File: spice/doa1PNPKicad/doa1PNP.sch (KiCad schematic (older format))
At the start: 27 parts, among them Q1 BC547, Q2 BC557, Q3 BC557, Q4 BC557, Q5 BC547, Q6 BC557, Q7 BC547

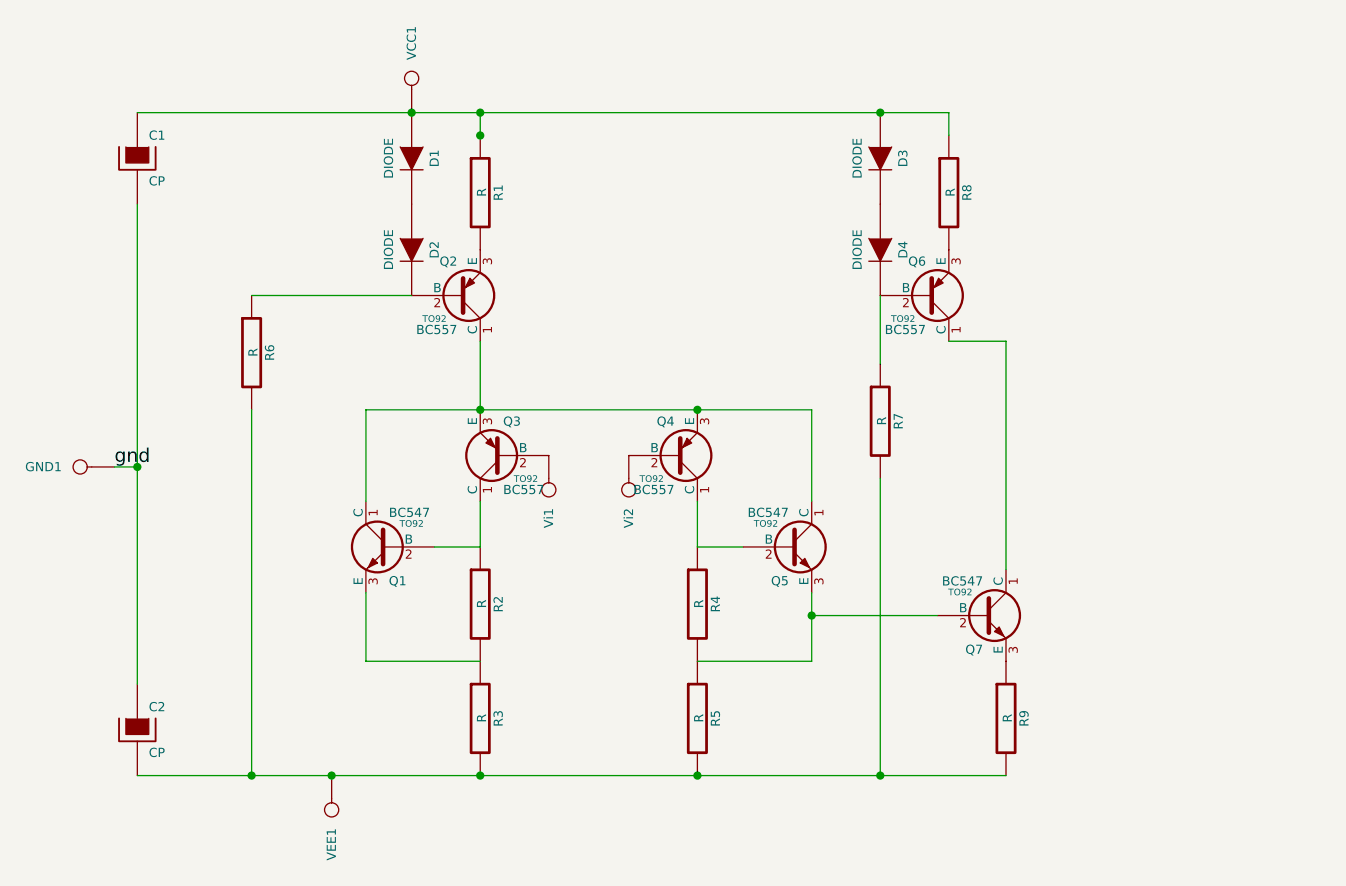
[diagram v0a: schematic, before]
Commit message: multiple current source doa1PNP
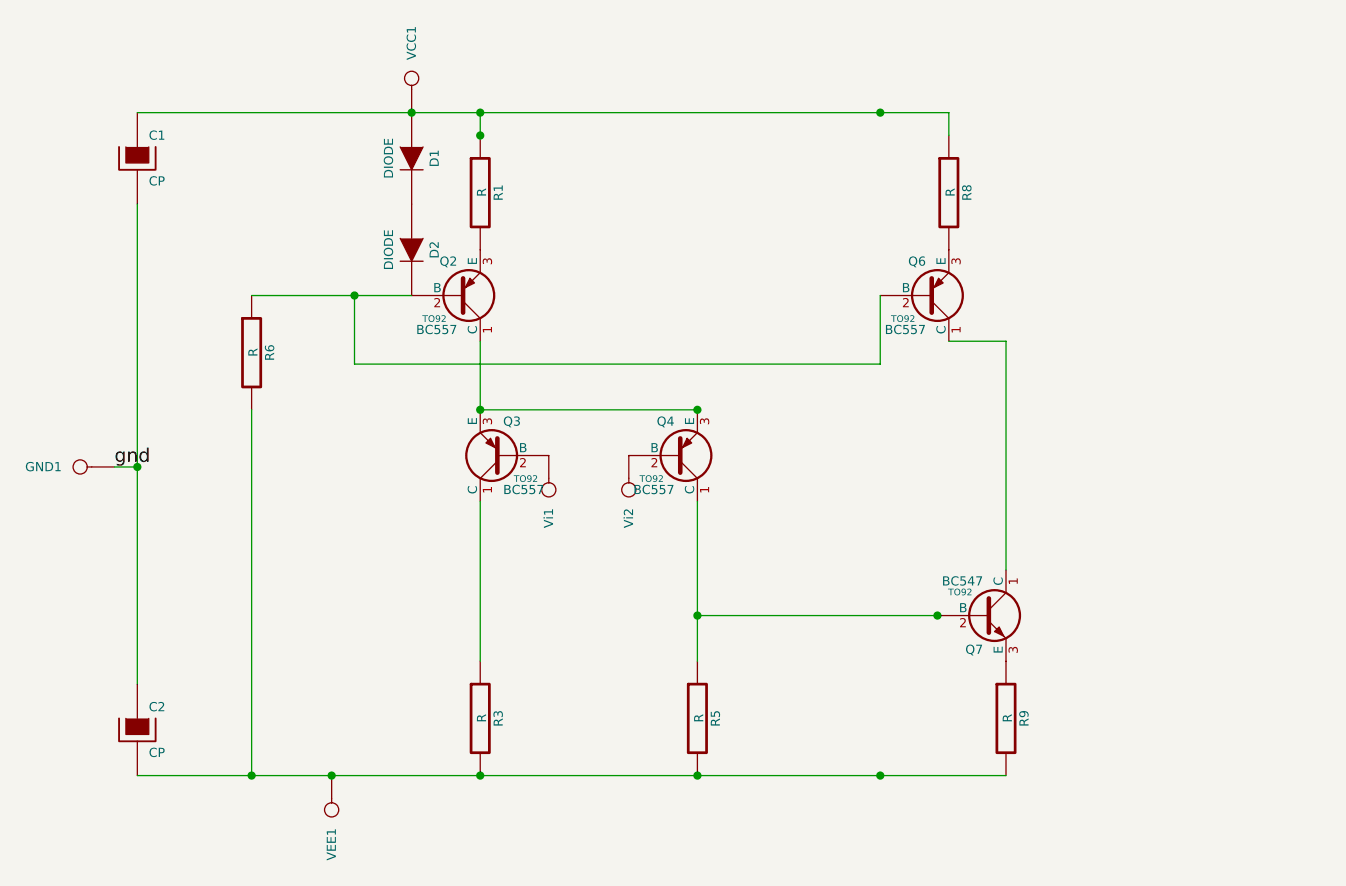
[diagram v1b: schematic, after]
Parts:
- removed D3, D4: DIODE, ~, symbol DIODE
- removed Q1, Q5: BC547, TO92, symbol BC547
- removed R2, R4, R7: R, ~, symbol R
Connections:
- net at Q3.1 (C): now also R3.1
- net at Q4.1 (C): now also Q7.2 (B), R5.1
- net at D2.2 (K), Q2.2 (B), R6.1: now also Q6.2 (B)
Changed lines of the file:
@@
 Sheet 1 1
 Title ""
-Date "23 may 2017"
+Date "24 may 2017"
 Rev ""
 Comp ""
@@
 $EndComp
 $Comp
-L BC547 Q1
-U 1 1 59244430
-P 3100 3400
-F 0 "Q1" H 3100 3251 40  0000 R CNN
-F 1 "BC547" H 3100 3550 40  0000 R CNN
-F 2 "TO92" H 3000 3502 29  0000 C CNN
-F 3 "" H 3100 3400 60  0000 C CNN
-	1    3100 3400
-	-1   0    0    -1
-$EndComp
-$Comp
-L R R2
-U 1 1 5924445D
-P 3500 3650
-F 0 "R2" V 3580 3650 40  0000 C CNN
-F 1 "R" V 3507 3651 40  0000 C CNN
-F 2 "~" V 3430 3650 30  0000 C CNN
-F 3 "~" H 3500 3650 30  0000 C CNN
-	1    3500 3650
-	1    0    0    -1
-$EndComp
-$Comp
 L DIODE D2
 U 1 1 59244502
@@
 $EndComp
 $Comp
-L BC547 Q5
-U 1 1 59244631
-P 4850 3400
-F 0 "Q5" H 4850 3251 40  0000 R CNN
-F 1 "BC547" H 4850 3550 40  0000 R CNN
-F 2 "TO92" H 4750 3502 29  0000 C CNN
-F 3 "" H 4850 3400 60  0000 C CNN
-	1    4850 3400
-	1    0    0    -1
-$EndComp
-$Comp
-L R R4
-U 1 1 5924468A
-P 4450 3650
-F 0 "R4" V 4530 3650 40  0000 C CNN
-F 1 "R" V 4457 3651 40  0000 C CNN
-F 2 "~" V 4380 3650 30  0000 C CNN
-F 3 "~" H 4450 3650 30  0000 C CNN
-	1    4450 3650
-	1    0    0    -1
-$EndComp
-$Comp
 L R R5
 U 1 1 59244760
@@
 Wire Wire Line
 	3500 2500 3500 2800
-Wire Wire Line
-	3000 2800 3000 3200
 Connection ~ 3500 2800
 Wire Wire Line
-	3300 3400 3500 3400
-Wire Wire Line
-	3000 3600 3000 3900
-Wire Wire Line
-	3000 3900 3500 3900
-Wire Wire Line
-	3500 3400 3500 3200
-Wire Wire Line
-	4450 3200 4450 3400
-Wire Wire Line
-	4450 3400 4650 3400
-Wire Wire Line
-	4950 2800 4950 3200
+	3500 3900 3500 3200
+Wire Wire Line
+	4450 3200 4450 3900
 Connection ~ 4450 2800
-Wire Wire Line
-	4950 3600 4950 3900
-Wire Wire Line
-	4950 3900 4450 3900
-Wire Wire Line
-	3000 2800 4950 2800
 Wire Wire Line
 	2000 4400 5800 4400
@@
 $EndComp
 $Comp
-L DIODE D4
-U 1 1 59247396
-P 5250 2100
-F 0 "D4" H 5250 2200 40  0000 C CNN
-F 1 "DIODE" H 5250 2000 40  0000 C CNN
-F 2 "~" H 5250 2100 60  0000 C CNN
-F 3 "~" H 5250 2100 60  0000 C CNN
-	1    5250 2100
-	0    1    1    0
-$EndComp
-$Comp
-L DIODE D3
-U 1 1 5924739C
-P 5250 1700
-F 0 "D3" H 5250 1800 40  0000 C CNN
-F 1 "DIODE" H 5250 1600 40  0000 C CNN
-F 2 "~" H 5250 1700 60  0000 C CNN
-F 3 "~" H 5250 1700 60  0000 C CNN
-	1    5250 1700
-	0    1    1    0
-$EndComp
-$Comp
 L R R8
 U 1 1 592473A2
@@
 	5250 2300 5250 2300
 Connection ~ 5250 1500
-$Comp
-L R R7
-U 1 1 59247477
-P 5250 2850
-F 0 "R7" V 5330 2850 40  0000 C CNN
-F 1 "R" V 5257 2851 40  0000 C CNN
-F 2 "~" V 5180 2850 30  0000 C CNN
-F 3 "~" H 5250 2850 30  0000 C CNN
-	1    5250 2850
-	1    0    0    -1
-$EndComp
 Wire Wire Line
 	5250 2300 5250 2600
-Wire Wire Line
-	5250 4400 5250 3100
 Connection ~ 4450 4400
 $Comp
@@
 Connection ~ 5250 4400
 Wire Wire Line
-	5500 3700 4950 3700
-Connection ~ 4950 3700
+	5500 3700 4450 3700
 Wire Wire Line
 	5800 3500 5800 2500
@@
 Connection ~ 3500 1600
 Connection ~ 3500 1500
+Connection ~ 5500 3700
+Connection ~ 4450 3700
+Wire Wire Line
+	3500 2800 4450 2800
+Wire Wire Line
+	2950 2300 2950 2600
+Wire Wire Line
+	2950 2600 5250 2600
+Connection ~ 2950 2300
 $EndSCHEMATC

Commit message: kicad out stage
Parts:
- added Q1, Q5: BC557, TO92, symbol BC557
- added R2: R, ~, symbol R
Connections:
- net at D2.2 (K), Q2.2 (B), Q6.2 (B)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: now also Q1.2 (B)
- net at C1.1, D1.1 (A), R1.1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: now also R2.1
- net at C2.2, R3.2, R5.2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: now also Q5.1 (C)
- net at Q6.1 (C), Q7.1 (C): now also Q5.2 (B)
- new net: Q1.1 (C), Q5.3 (E)
- new net: Q1.3 (E), R2.2
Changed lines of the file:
@@
 $EndComp
 Wire Wire Line
-	2000 1500 5550 1500
+	2000 1500 6800 1500
 Wire Wire Line
 	3500 1500 3500 1600
@@
 Connection ~ 4450 2800
 Wire Wire Line
-	2000 4400 5800 4400
+	2000 4400 6800 4400
 $Comp
 L CONN_1 Vi1
@@
 	2950 2300 2950 2600
 Wire Wire Line
-	2950 2600 5250 2600
+	2950 2600 6500 2600
 Connection ~ 2950 2300
+$Comp
+L BC557 Q5
+U 1 1 592586E3
+P 6700 4000
+F 0 "Q5" H 6700 3851 40  0000 R CNN
+F 1 "BC557" H 6700 4150 40  0000 R CNN
+F 2 "TO92" H 6600 4102 29  0000 C CNN
+F 3 "" H 6700 4000 60  0000 C CNN
+	1    6700 4000
+	1    0    0    1
+$EndComp
+$Comp
+L BC557 Q1
+U 1 1 592586EC
+P 6700 2350
+F 0 "Q1" H 6700 2201 40  0000 R CNN
+F 1 "BC557" H 6700 2500 40  0000 R CNN
+F 2 "TO92" H 6600 2452 29  0000 C CNN
+F 3 "" H 6700 2350 60  0000 C CNN
+	1    6700 2350
+	1    0    0    1
+$EndComp
+Wire Wire Line
+	6800 4400 6800 4200
+Connection ~ 5800 4400
+Wire Wire Line
+	5800 3350 6500 3350
+Wire Wire Line
+	6500 3350 6500 4000
+Connection ~ 5800 3350
+Wire Wire Line
+	6500 2600 6500 2350
+Connection ~ 5250 2600
+Wire Wire Line
+	6800 2550 6800 3800
+$Comp
+L R R2
+U 1 1 5925881A
+P 6800 1900
+F 0 "R2" V 6880 1900 40  0000 C CNN
+F 1 "R" V 6807 1901 40  0000 C CNN
+F 2 "~" V 6730 1900 30  0000 C CNN
+F 3 "~" H 6800 1900 30  0000 C CNN
+	1    6800 1900
+	1    0    0    -1
+$EndComp
+Wire Wire Line
+	6800 1500 6800 1650
+Connection ~ 5550 1500
 $EndSCHEMATC

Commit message: layout
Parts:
- added Out1: CONN_1, symbol CONN_1
- renumbered Q1 to Q1CS3, Q2 to Q2CS1, Q6 to Q6CS2
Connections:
- net at Q1CS3.1 (C), Q5.3 (E): now also Out1.1
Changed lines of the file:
@@
 $EndComp
 $Comp
-L BC557 Q2
+L BC557 Q2CS1
 U 1 1 5924441E
 P 3400 2300
-F 0 "Q2" H 3400 2151 40  0000 R CNN
+F 0 "Q2CS1" H 3400 2151 40  0000 R CNN
 F 1 "BC557" H 3400 2450 40  0000 R CNN
 F 2 "TO92" H 3300 2402 29  0000 C CNN
@@
 $EndComp
 $Comp
-L BC557 Q6
+L BC557 Q6CS2
 U 1 1 59247390
 P 5450 2300
-F 0 "Q6" H 5450 2151 40  0000 R CNN
+F 0 "Q6CS2" H 5450 2151 40  0000 R CNN
 F 1 "BC557" H 5450 2450 40  0000 R CNN
 F 2 "TO92" H 5350 2402 29  0000 C CNN
@@
 $EndComp
 $Comp
-L BC557 Q1
+L BC557 Q1CS3
 U 1 1 592586EC
 P 6700 2350
-F 0 "Q1" H 6700 2201 40  0000 R CNN
+F 0 "Q1CS3" H 6700 2201 40  0000 R CNN
 F 1 "BC557" H 6700 2500 40  0000 R CNN
 F 2 "TO92" H 6600 2452 29  0000 C CNN
@@
 	6800 1500 6800 1650
 Connection ~ 5550 1500
+$Comp
+L CONN_1 Out1
+U 1 1 5925B523
+P 6950 3050
+F 0 "Out1" H 7030 3050 40  0000 L CNN
+F 1 "CONN_1" H 6950 3105 30  0001 C CNN
+F 2 "" H 6950 3050 60  0000 C CNN
+F 3 "" H 6950 3050 60  0000 C CNN
+	1    6950 3050
+	1    0    0    -1
+$EndComp
+Connection ~ 6800 3050
 $EndSCHEMATC
